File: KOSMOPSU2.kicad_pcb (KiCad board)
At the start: 2 copper layers, 153.7 x 73.9 mm, 31 parts, among them J1 Conn_01x03_Male, J2 Conn_02x05_Odd_Even, J3 Conn_01x03_Male, T1 Myrra 44440 Transformer 240V, U1 L7812, U2 L7912

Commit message: Cap Update
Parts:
- T1: value Myrra 44440 Transformer 240V -> Myrra 44441 Transformer 240V
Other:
- board text added: "Myrra 44453 Transformer 117V"
- board text removed: "Myrra 44452 Transformer 115V"
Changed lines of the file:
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@@
       (effects (font (size 1 1) (thickness 0.15)))
     )
-    (fp_text value "Myrra 44440 Transformer 240V " (at 32.372 2.14 90) (layer F.SilkS)
+    (fp_text value "Myrra 44441 Transformer 240V " (at 32.372 2.14 90) (layer F.SilkS)
       (effects (font (size 3 2) (thickness 0.15)))
     )
@@
     )
   )
-  (gr_text "Myrra 44452 Transformer 115V " (at 54.864 86.868 90) (layer F.SilkS)
+  (gr_text "Myrra 44453 Transformer 117V " (at 54.864 86.868 90) (layer F.SilkS)
     (effects (font (size 3 2) (thickness 0.15)))
   )

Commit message: Cap Update
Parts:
- T1: value Myrra 44441 Transformer 240V -> Myrra 44440 Transformer 240V
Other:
- board text added: "Myrra 44452 Transformer 117V"
- board text removed: "Myrra 44453 Transformer 117V"
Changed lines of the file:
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@@
       (effects (font (size 1 1) (thickness 0.15)))
     )
-    (fp_text value "Myrra 44441 Transformer 240V " (at 32.372 2.14 90) (layer F.SilkS)
+    (fp_text value "Myrra 44440 Transformer 240V " (at 32.372 2.14 90) (layer F.SilkS)
       (effects (font (size 3 2) (thickness 0.15)))
     )
@@
     )
   )
-  (gr_text "Myrra 44453 Transformer 117V " (at 54.864 86.868 90) (layer F.SilkS)
+  (gr_text "Myrra 44452 Transformer 117V " (at 54.864 86.868 90) (layer F.SilkS)
     (effects (font (size 3 2) (thickness 0.15)))
   )

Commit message: -12V header Fix
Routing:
- net -12V: track 58.1 -> 60.6 mm

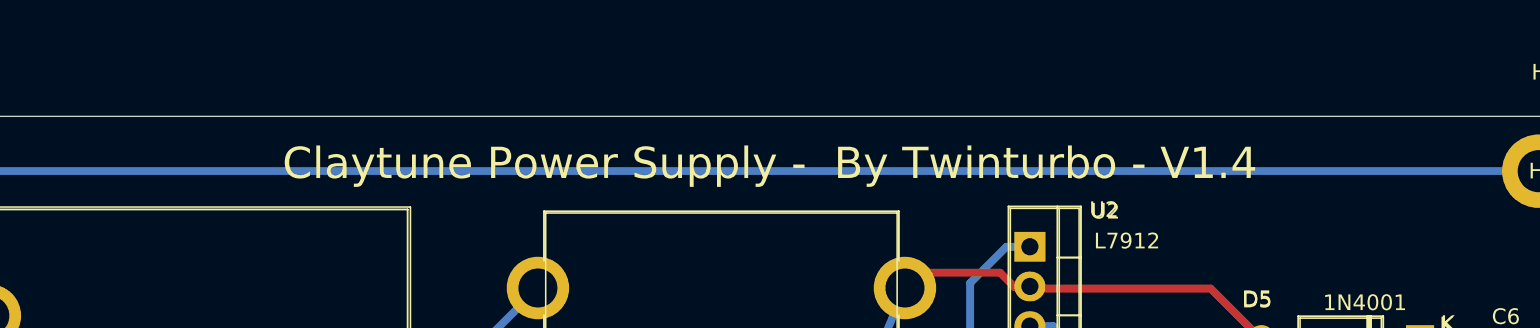
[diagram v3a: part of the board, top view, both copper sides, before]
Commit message: -12V header Fix V1.5
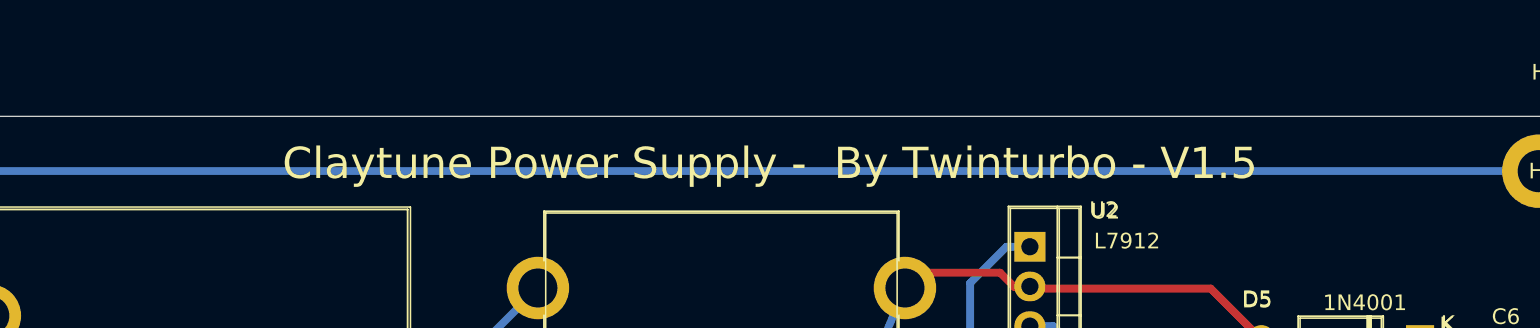
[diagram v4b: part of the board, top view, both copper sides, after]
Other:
- board text added: "Claytune Power Supply - By Twinturbo - V1.5"
- board text removed: "Claytune Power Supply - By Twinturbo - V1.4"
